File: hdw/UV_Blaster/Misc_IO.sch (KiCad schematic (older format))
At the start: 27 parts, among them SW901 Cap_Touch, U902 AT42QT1010-TSHR

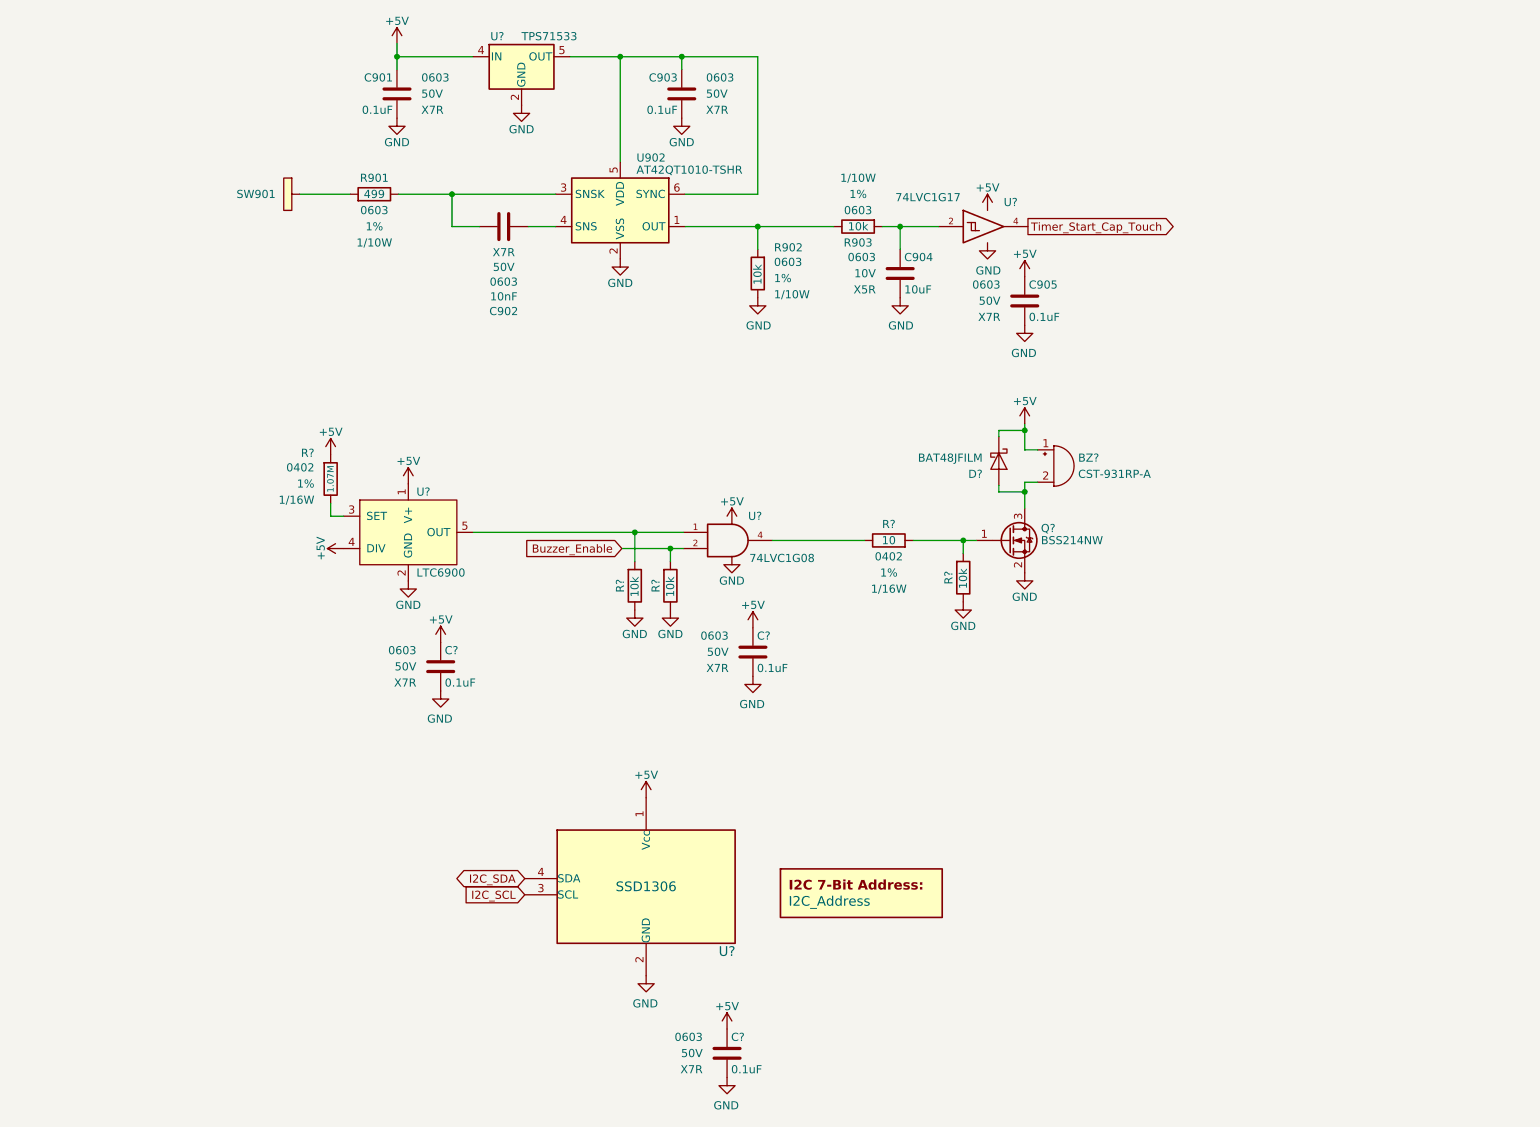
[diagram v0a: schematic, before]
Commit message: More sch work, netlist, part numbers, footprints
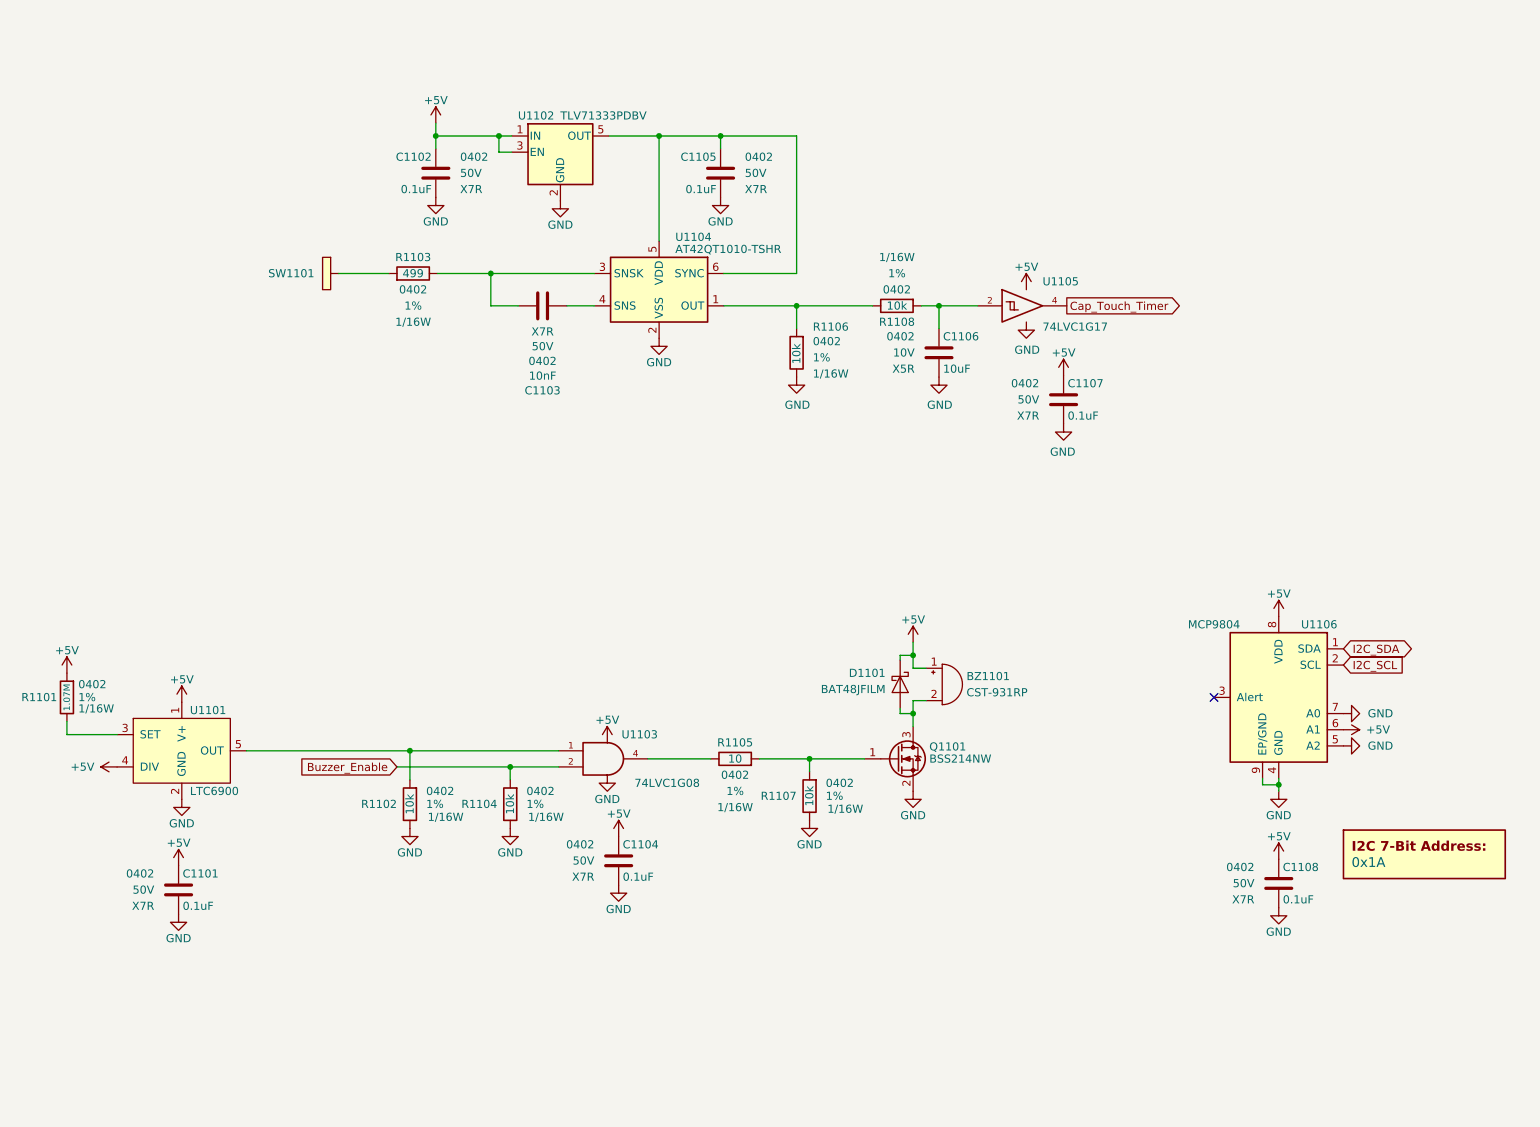
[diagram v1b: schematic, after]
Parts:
- removed BZ?: CST-931RP-A, Buzzer_Beeper:MagneticBuzzer_CUI_CST-931RP-A, symbol Device:Buzzer
- removed C901, C903, C905, C? (x3): 0.1uF, Capacitors_SMD:C_0603, symbol Custom_Library:C_Custom
- removed C902: 10nF, Capacitors_SMD:C_0603, symbol Custom_Library:C_Custom
- removed C904: 10uF, Capacitors_SMD:C_0603, symbol Custom_Library:C_Custom
- removed D?: BAT48JFILM, Diode_SMD:D_SOD-323, symbol Diode:BAT48JFILM
- removed DOC?: I2C_Address, symbol Custom_Library:I2C_Address
- removed Q?: BSS214NW, TO_SOT_Packages_SMD:SOT-323_SC-70, symbol Transistor_FET:BSS214NW
- removed R901: 499, Resistors_SMD:R_0603, symbol Custom_Library:R_Custom
- removed R902, R903, R? (x3): 10k, Resistors_SMD:R_0603, symbol Custom_Library:R_Custom
- removed R?: 1.07M, Resistors_SMD:R_0402, symbol Custom_Library:R_Custom
- removed R?: 10, Resistors_SMD:R_0402, symbol Custom_Library:R_Custom
- removed SW901: Cap_Touch, Custom Footprints Library:Capacitive_Touch_Pad, symbol Custom_Library:Cap_Touch
- removed U902: AT42QT1010-TSHR, TO_SOT_Packages_SMD:SOT-23-6, symbol Sensor_Touch:AT42QT1010-TSHR
- removed U?: TPS71533, Package_TO_SOT_SMD:SOT-353_SC-70-5, symbol Regulator_Linear:TPS71533__SC70
- removed U?: 74LVC1G17, TO_SOT_Packages_SMD:SOT-353_SC-70-5, symbol Custom_Library:74LVC1G17_Power
- removed U?: LTC6900, Package_TO_SOT_SMD:SOT-23-5, symbol Custom_Library:LTC6900
- removed U?: 74LVC1G08, symbol Custom_Library:74LVC1G08_Power
- removed U?: SSD1306, symbol Custom_Library:SSD1306
- added BZ1101: CST-931RP, Buzzer_Beeper:MagneticBuzzer_CUI_CST-931RP-A, symbol Device:Buzzer
- added C1101, C1102, C1104, C1105, C1107, C1108: 0.1uF, Capacitors_SMD:C_0402, symbol Custom_Library:C_Custom
- added C1103: 10nF, Capacitors_SMD:C_0402, symbol Custom_Library:C_Custom
- added C1106: 10uF, Capacitors_SMD:C_0402, symbol Custom_Library:C_Custom
- added D1101: BAT48JFILM, Diode_SMD:D_SOD-323, symbol Diode:BAT48JFILM
- added DOC1101: 0x1A, symbol Custom_Library:I2C_Address
- added Q1101: BSS214NW, TO_SOT_Packages_SMD:SOT-323_SC-70, symbol Transistor_FET:BSS214NW
- added R1101: 1.07M, Resistors_SMD:R_0402, symbol Custom_Library:R_Custom
- added R1102, R1104, R1106, R1107, R1108: 10k, Resistors_SMD:R_0402, symbol Custom_Library:R_Custom
- added R1103: 499, Resistors_SMD:R_0402, symbol Custom_Library:R_Custom
- added R1105: 10, Resistors_SMD:R_0402, symbol Custom_Library:R_Custom
- added SW1101: Cap_Touch, Custom Footprints Library:Capacitive_Touch_Pad, symbol Custom_Library:Cap_Touch
- added U1101: LTC6900, Package_TO_SOT_SMD:SOT-23-5, symbol Custom_Library:LTC6900
- added U1102: TLV71333PDBV, Package_TO_SOT_SMD:SOT-23-5, symbol Regulator_Linear:TLV71333PDBV
- added U1103: 74LVC1G08, Package_TO_SOT_SMD:SOT-353_SC-70-5, symbol Custom_Library:74LVC1G08_Power
- added U1104: AT42QT1010-TSHR, TO_SOT_Packages_SMD:SOT-23-6, symbol Sensor_Touch:AT42QT1010-TSHR
- added U1105: 74LVC1G17, TO_SOT_Packages_SMD:SOT-353_SC-70-5, symbol Custom_Library:74LVC1G17_Power
- added U1106: MCP9804, Package_DFN_QFN:DFN-8-1EP_3x2mm_P0.5mm_EP1.3x1.5mm, symbol Sensor_Temperature:MCP9804_DFN
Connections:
- net +5V: now also BZ1101.1 (-), C1101.1, C1102.1, C1104.1, C1107.1, C1108.1, D1101.1 (K), R1101.1, U1101.1 (V+), U1101.4 (DIV), U1102.1 (IN), U1102.3 (EN), U1103.5 (VCC), U1105.5 (VCC), U1106.6 (A1), U1106.8 (VDD)
- net Buzzer_Enable: now also R1104.1, U1103.2
- net GND: now also C1101.2, C1102.2, C1104.2, C1105.2, C1106.2, C1107.2, C1108.2, Q1101.2 (S), R1102.2, R1104.2, R1106.2, R1107.2, U1101.2 (GND), U1102.2 (GND), U1103.3 (GND), U1104.2 (VSS), U1105.3 (GND), U1106.4 (GND), U1106.5 (A2), U1106.7 (A0), U1106.9 (EP/GND)
- net I2C_SCL: now also U1106.2 (SCL)
- net I2C_SDA: now also U1106.1 (SDA)
- new net: R1106.1, R1108.2, U1104.1 (OUT)
- new net: C1103.2, R1103.2, U1104.3 (SNSK)
- new net: C1103.1, U1104.4 (SNS)
- new net: C1105.1, U1102.5 (OUT), U1104.5 (VDD), U1104.6 (SYNC)
- new net: R1103.1, SW1101.1 (TP)
- new net: C1106.1, R1108.1, U1105.2
- new net: R1101.2, U1101.3 (SET)
- new net: R1102.1, U1101.5 (OUT), U1103.1
- new net: R1105.2, U1103.4
- new net: Q1101.1 (G), R1105.1, R1107.1
- new net: BZ1101.2 (+), D1101.2 (A), Q1101.3 (D)
- new net Cap_Touch_Timer: U1105.4
- no-connect marks 0 -> 1
